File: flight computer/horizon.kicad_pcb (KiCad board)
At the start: 4 copper layers, 50.8 x 95.7 mm, 151 parts, among them J1 Micro_SD_Card_Det1, J10 Conn_01x02_Pin, J11 USB_C_Receptacle_USB2.0_16P, J12 Conn_01x04, J13 1x3 servo, J14 1x3 servo, J15 arming terminal, J16 arming terminal, J17 H9161TR-ND, J18 Conn_02x03_Counter_Clockwise, J19 Screw_Terminal_01x02, J20 Screw_Terminal_01x02, J21 Conn_02x03_Counter_Clockwise, J3 H9161TR-ND, J4 H9161TR-ND, J5 Screw_Term, J6 1x3 servo, J9 1x3 servo, Q2 DMG2301L, Q7 BSS138, Q8 IRLML6402, Q9 IRLML6402, SW1 CK_KMS2xxG, U1 MMCU, U10 LSM6DS3, U11 BGM220SC12WGA2R, U13 LTC4412xS6, U15 AP2112K-3.3, U16 SX1262IMLTRT, U17 PE4259, U2 MKL02Z32VFG4, U3 TPS61200DRC, U5 LPS22HB, U6 GPS, U8 NAND, U9 TPS82130, Y1 Crystal, Y2 32MHz

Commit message: i forgot what i did
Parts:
- moved Q7 17.3 mm to (187.5, 139.7)
- moved R72 17.3 mm to (191.2, 138.0)
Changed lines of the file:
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@@
 			(psa4output no)
 			(plot_black_and_white yes)
+			(plotinvisibletext no)
 			(sketchpadsonfab no)
 			(plotpadnumbers no)
@@
 	(footprint "Package_TO_SOT_SMD:SOT-23"
 		(layer "F.Cu")
-		(at 204.6175 141.79)
+		(at 187.4575 139.66)
 		(descr "SOT, 3 Pin (JEDEC TO-236 Var AB https://www.jedec.org/document_search?search_api_views_fulltext=TO-236), generated with kicad-footprint-generator ipc_gullwing_generator.py")
 		(tags "SOT TO_SOT_SMD")
@@
 	(footprint "Resistor_SMD:R_0603_1608Metric"
 		(layer "F.Cu")
-		(at 208.38 140.125 90)
+		(at 191.22 137.995 90)
 		(descr "Resistor SMD 0603 (1608 Metric), square (rectangular) end terminal, IPC_7351 nominal, (Body size source: IPC-SM-782 page 72, https://www.pcb-3d.com/wordpress/wp-content/uploads/ipc-sm-782a_amendment_1_and_2.pdf), generated with kicad-footprint-generator")
 		(tags "resistor")

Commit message: gotta get those daily commits in
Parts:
- moved R55 34.6 mm to (193.3, 88.6), turned to 0 degrees
- moved C15 33.7 mm to (191.0, 89.5), turned to 90 degrees
- moved R54 29.4 mm to (191.0, 92.6), turned to 90 degrees
- moved J1 29.2 mm to (196.5, 92.4), turned to 180 degrees
- moved U8 29.2 mm to (196.5, 92.4), turned to 180 degrees
- moved R12 28.8 mm to (202.0, 93.9), turned to 90 degrees
- moved R56 25.9 mm to (204.3, 97.2), turned to 90 degrees
- moved C47 10.7 mm to (180.7, 95.4)
- moved FL1 10.7 mm to (184.7, 95.6)
- moved R8 10.7 mm to (187.2, 89.0)
- moved C46 10.7 mm to (187.1, 92.1)
- moved C48 10.7 mm to (182.2, 95.4)
- moved L10 10.7 mm to (183.0, 97.7)
- moved U17 10.7 mm to (184.9, 92.7)
- moved C49 10.7 mm to (184.9, 89.6)
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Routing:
- net +3.3V: track 71.8 -> 141.7 mm
- net GND: track 119.2 -> 121.6 mm, vias 78 -> 80
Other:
- board size 50.8 x 95.7 mm -> 50.8 x 78 mm

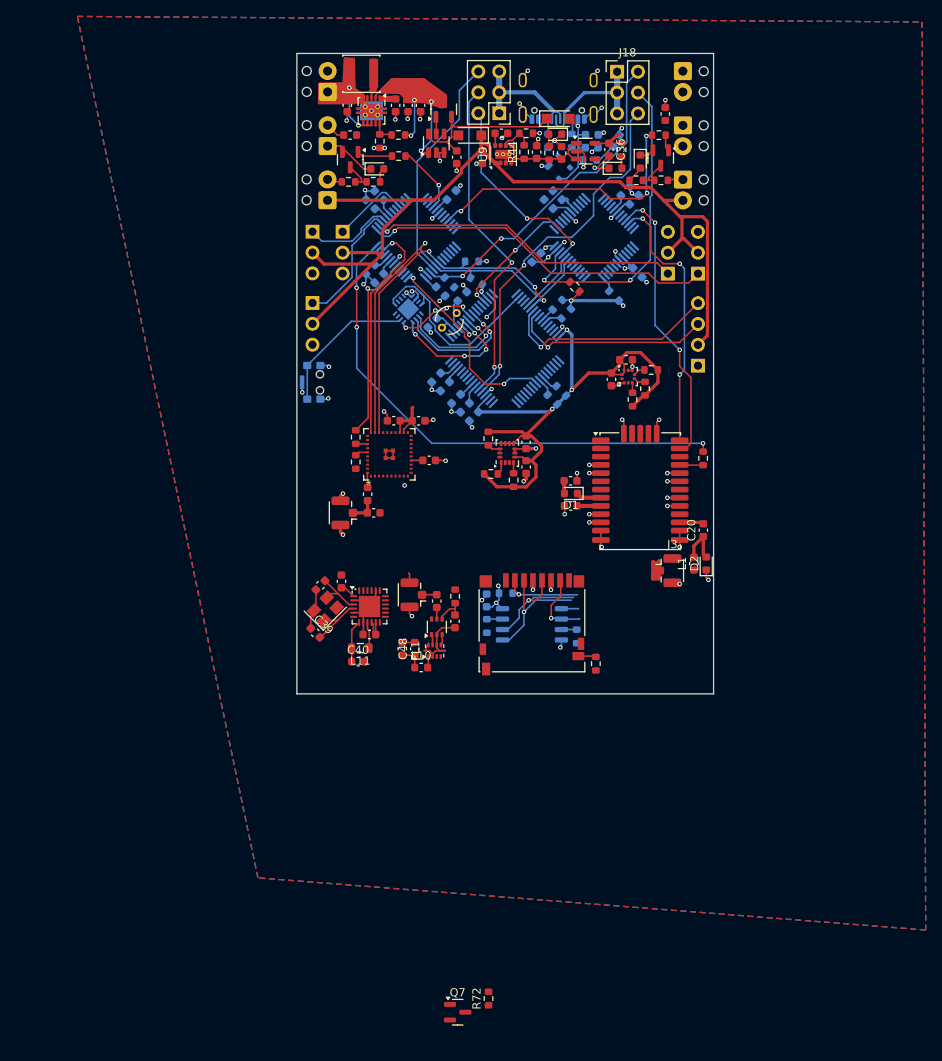
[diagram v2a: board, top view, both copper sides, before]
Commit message: work and updated from schematic
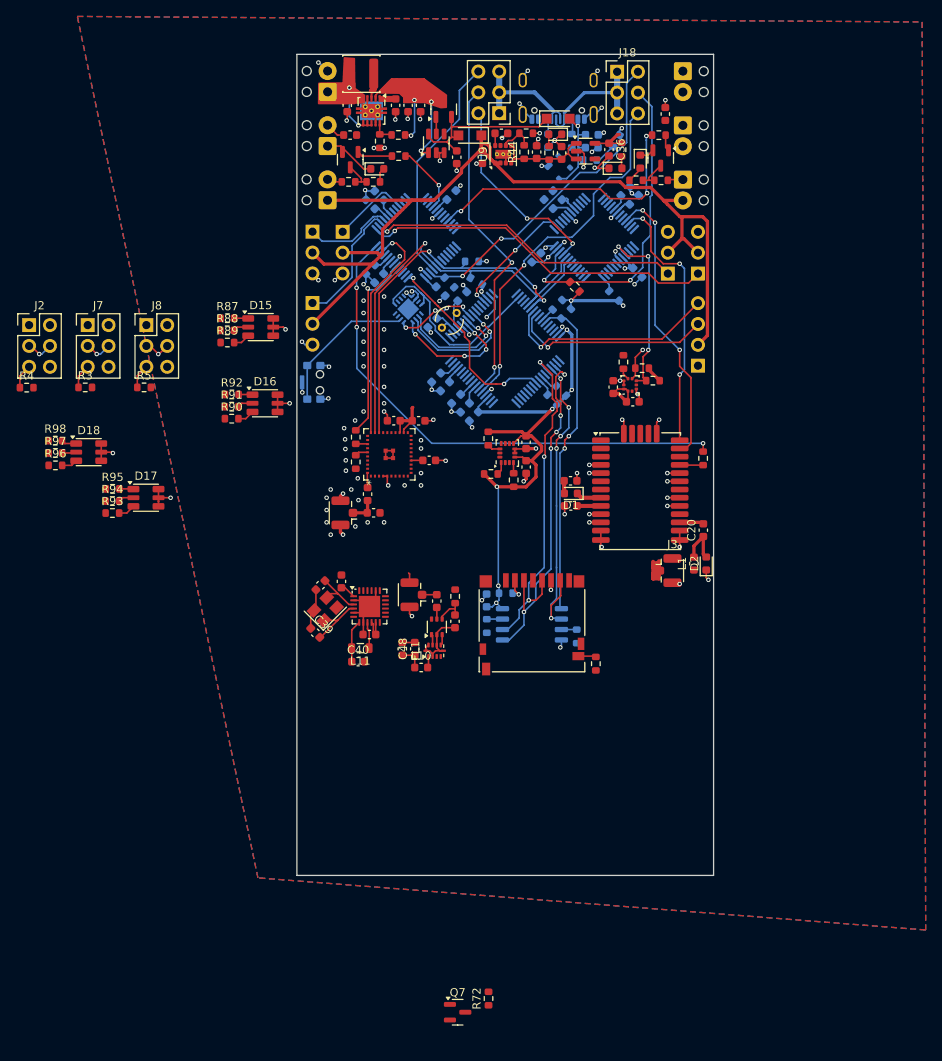
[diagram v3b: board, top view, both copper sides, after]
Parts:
- added D15: SMLVN6RGB, LED_SMD:LED_ROHM_SMLVN6, F.Cu at (163.5, 56.2)
- added D16: SMLVN6RGB, LED_SMD:LED_ROHM_SMLVN6, F.Cu at (164.0, 65.5)
- added D17: SMLVN6RGB, LED_SMD:LED_ROHM_SMLVN6, F.Cu at (149.5, 77.0)
- added D18: SMLVN6RGB, LED_SMD:LED_ROHM_SMLVN6, F.Cu at (142.5, 71.5)
- added J2: Conn_02x03_Counter_Clockwise, Connector_PinHeader_2.54mm:PinHeader_2x03_P2.54mm_Vertical, F.Cu at (135.3, 56.0)
- added J7: Conn_02x03_Counter_Clockwise, Connector_PinHeader_2.54mm:PinHeader_2x03_P2.54mm_Vertical, F.Cu at (142.4, 56.0)
- added J8: Conn_02x03_Counter_Clockwise, Connector_PinHeader_2.54mm:PinHeader_2x03_P2.54mm_Vertical, F.Cu at (149.5, 56.0)
- added R3: 10k, Resistor_SMD:R_0603_1608Metric, F.Cu at (142.1, 63.6)
- added R4: 10k, Resistor_SMD:R_0603_1608Metric, F.Cu at (135.0, 63.6)
- added R5: 10k, Resistor_SMD:R_0603_1608Metric, F.Cu at (149.3, 63.6)
- added R87: 220, Resistor_SMD:R_0603_1608Metric, F.Cu at (159.4, 55.1)
- added R88: 220, Resistor_SMD:R_0603_1608Metric, F.Cu at (159.4, 56.6)
- added R89: 220, Resistor_SMD:R_0603_1608Metric, F.Cu at (159.4, 58.1)
- added R90: 220, Resistor_SMD:R_0603_1608Metric, F.Cu at (159.9, 67.4)
- added R91: 220, Resistor_SMD:R_0603_1608Metric, F.Cu at (159.9, 65.9)
- added R92: 220, Resistor_SMD:R_0603_1608Metric, F.Cu at (160.0, 64.4)
- added R93: 220, Resistor_SMD:R_0603_1608Metric, F.Cu at (145.4, 78.9)
- added R94: 220, Resistor_SMD:R_0603_1608Metric, F.Cu at (145.4, 77.4)
- added R95: 220, Resistor_SMD:R_0603_1608Metric, F.Cu at (145.4, 75.9)
- added R96: 220, Resistor_SMD:R_0603_1608Metric, F.Cu at (138.5, 73.1)
- added R97: 220, Resistor_SMD:R_0603_1608Metric, F.Cu at (138.5, 71.5)
- added R98: 220, Resistor_SMD:R_0603_1608Metric, F.Cu at (138.5, 70.0)
- moved C51 3.77 mm to (208.8, 65.3), turned to 180 degrees
- moved C50 3.68 mm to (206.4, 63.5), turned to -90 degrees
- moved R52 3.52 mm to (207.6, 60.5), turned to -90 degrees
- moved R53 3.38 mm to (211.2, 62.7), turned to 180 degrees
- moved R39 2.52 mm to (209.9, 61.2), turned to 180 degrees
- moved U5 1.04 mm to (208.5, 63.3), turned to 90 degrees
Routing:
- net CS_NAND MMCU: track 4.32 -> 39.6 mm, vias 0 -> 2
- net GND: track 121.6 -> 154.1 mm, vias 80 -> 127
- net NAND_MISO MMCU: track 8.61 -> 38.6 mm, vias 1 -> 5
- net NAND_MOSI MMCU: track 15.2 -> 42.8 mm, vias 1 -> 5
- net SPI0_SCK MMCU: track 14.5 -> 41.7 mm, vias 1 -> 3
- net MISO TMCU: track 2.77 -> 23.7 mm, vias 0 -> 3
- net CS_SD MMCU: track 11.7 -> 4.54 mm
- net +3.3V: track 141.7 -> 137.4 mm
- net nRESET MMCU: track 25.5 -> 28.5 mm
- net nRESET DMCU-1: track 0.00 -> 2.98 mm
- net nRESET DMCU-2: track 0.00 -> 2.96 mm
- net CS_BARO TMCU: track 1.44 -> 4.04 mm, vias 0 -> 1
- net Net-(D17-GA): track 0.00 -> 2.08 mm
- net Net-(D16-GA): track 0.00 -> 2.05 mm
- net Net-(D15-GA): track 0.00 -> 2.05 mm
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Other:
- board size 50.8 x 78 mm -> 50.8 x 100 mm

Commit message: review please before power rails
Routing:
- net +3.3V: track 137.4 -> 184.6 mm
- net GND: track 154.1 -> 160.3 mm, vias 127 -> 130
- net D+: track 15.7 -> 21.9 mm
- net D-: track 15.2 -> 20.2 mm
- net +5V: track 121.5 -> 117.5 mm
- net MISO TMCU: track 23.7 -> 21.4 mm
- net I2C0_SCL: track 53.4 -> 51.3 mm
- net D- DMCU-2: track 24.0 -> 22.5 mm
- net PTD4: track 23.9 -> 22.6 mm
- net I2C0_SDA: track 52.8 -> 51.5 mm
- net NAND_MOSI MMCU: track 42.8 -> 41.6 mm
- net mosfet2_signalfire: track 34.4 -> 33.4 mm
- net D- MMCU: track 40.4 -> 41.0 mm
- net D+ DMCU-2: track 39.6 -> 39.0 mm

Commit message: did a lot of wiring stuffs
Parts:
- moved C14 19.3 mm to (171.3, 107.0)
- moved C37 19.3 mm to (177.2, 113.0)
- moved C38 19.3 mm to (173.8, 106.5)
- moved C39 19.3 mm to (170.6, 112.8)
- moved C40 19.3 mm to (175.9, 116.3)
- moved C46 19.3 mm to (187.7, 111.4)
- moved C47 19.3 mm to (181.2, 114.7)
- moved C48 19.3 mm to (182.8, 114.7)
- moved C49 19.3 mm to (185.4, 108.9)
- moved FL1 19.3 mm to (185.2, 115.0)
- moved J4 19.3 mm to (182.6, 108.1)
- moved L10 19.3 mm to (183.5, 117.0)
- moved L11 19.3 mm to (176.1, 114.6)
- moved R8 19.3 mm to (187.7, 108.3)
- moved U16 19.3 mm to (177.2, 109.6)
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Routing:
- net +3.3V: track 184.6 -> 168.8 mm
- net NAND_MISO MMCU: track 38.6 -> 33.7 mm, vias 5 -> 3
- net CS_NAND MMCU: track 39.6 -> 35.0 mm
- net SPI0_SCK MMCU: track 41.2 -> 36.6 mm
- net NAND_MOSI MMCU: track 41.6 -> 38.0 mm, vias 5 -> 3
- net +5V: track 117.5 -> 114.6 mm
- net GND: track 160.3 -> 157.4 mm, vias 130 -> 132

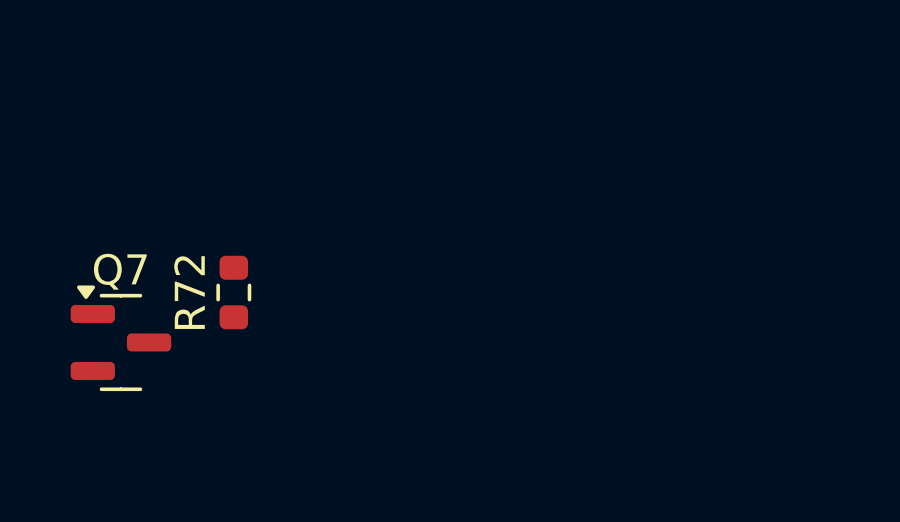
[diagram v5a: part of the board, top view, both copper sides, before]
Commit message: added buzzer footprint
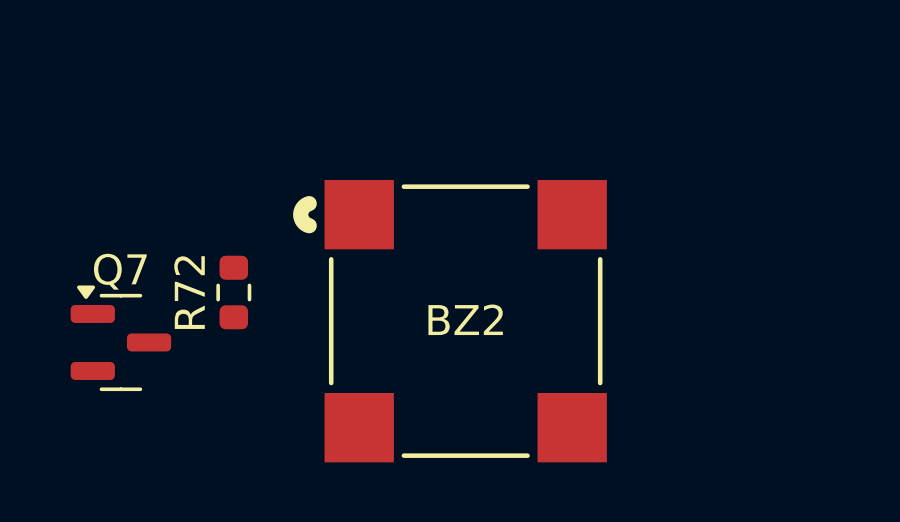
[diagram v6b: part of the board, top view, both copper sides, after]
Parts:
- added BZ2: Buzzer, Buzzer:MLT-8530_JHE, F.Cu at (198.9, 138.9)
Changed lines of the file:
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@@
 		)
+	)
+	(footprint "Buzzer:MLT-8530_JHE"
+		(layer "F.Cu")
+		(at 198.949999 138.949999)
+		(tags "MLT-8530 ")
+		(property "Reference" "BZ2"
+			(at 0 0 0)
+			(unlocked yes)
+			(layer "F.SilkS")
+			(effects
+				(font
+					(size 1 1)
+					(thickness 0.15)
+				)
+			)
+		)
+		(property "Value" "Buzzer"
+			(at 0 0 0)
+			(unlocked yes)
+			(layer "F.Fab")
+			(effects
+				(font
+					(size 1 1)
+					(thickness 0.15)
+				)
+			)
+		)
+		(property "Datasheet" "MLT-8530"
+			(at 0 0 0)
+			(layer "F.Fab")
+			(hide yes)
+			(effects
+				(font
+					(size 1.27 1.27)
+					(thickness 0.15)
+				)
+			)
+		)
+		(property "Description" "Buzzer, polarized"
+			(at 0 0 0)
+			(layer "F.Fab")
+			(hide yes)
+			(effects
+				(font
+					(size 1.27 1.27)
+					(thickness 0.15)
+				)
+			)
+		)
+		(property ki_fp_filters "MLT-8530_JHE")
+		(sheetname "/sensors/")
+		(sheetfile "sensor.kicad_sch")
+		(attr smd)
+		(fp_line
+			(start -4.4831 -2.061561)
+			(end -4.4831 2.061561)
+			(stroke
+				(width 0.1524)
+				(type solid)
+			)
+			(layer "F.SilkS")
+		)
+		(fp_line
+			(start -2.061561 4.4831)
+			(end 2.061561 4.4831)
+			(stroke
+				(width 0.1524)
+				(type solid)
+			)
+			(layer "F.SilkS")
+		)
+		(fp_line
+			(start 2.061561 -4.4831)
+			(end -2.061561 -4.4831)
+			(stroke
+				(width 0.1524)
+				(type solid)
+			)
+			(layer "F.SilkS")
+		)
+		(fp_line
+			(start 4.4831 2.061561)
+			(end 4.4831 -2.061561)
+			(stroke
+				(width 0.1524)
+				(type solid)
+			)
+			(layer "F.SilkS")
+		)
+		(fp_arc
+			(start -5.21624 -3.181857)
+			(mid -5.4991 -3.55)
+			(end -5.21624 -3.918144)
+			(stroke
+				(width 0.508)
+				(type solid)
+			)
+			(layer "F.SilkS")
+		)
+		(fp_circle
+			(center -5.1181 -3.55)
+			(end -4.7371 -3.55)
+			(stroke
+				(width 0.508)
+				(type solid)
+			)
+			(fill no)
+			(layer "B.SilkS")
+		)
+		(fp_line
+			(start -4.9597 -4.9597)
+			(end -4.9597 4.9597)
+			(stroke
+				(width 0.1524)
+				(type solid)
+			)
+			(layer "F.CrtYd")
+		)
+		(fp_line
+			(start -4.9597 4.9597)
+			(end 4.9597 4.9597)
+			(stroke
+				(width 0.1524)
+				(type solid)
+			)
+			(layer "F.CrtYd")
+		)
+		(fp_line
+			(start 4.9597 -4.9597)
+			(end -4.9597 -4.9597)
+			(stroke
+				(width 0.1524)
+				(type solid)
+			)
+			(layer "F.CrtYd")
+		)
+		(fp_line
+			(start 4.9597 4.9597)
+			(end 4.9597 -4.9597)
+			(stroke
+				(width 0.1524)
+				(type solid)
+			)
+			(layer "F.CrtYd")
+		)
+		(fp_line
+			(start -4.3561 -4.3561)
+			(end -4.3561 4.3561)
+			(stroke
+				(width 0.0254)
+				(type solid)
+			)
+			(layer "F.Fab")
+		)
+		(fp_line
+			(start -4.3561 4.3561)
+			(end 4.3561 4.3561)
+			(stroke
+				(width 0.0254)
+				(type solid)
+			)
+			(layer "F.Fab")
+		)
+		(fp_line
+			(start 4.3561 -4.3561)
+			(end -4.3561 -4.3561)
+			(stroke
+				(width 0.0254)
+				(type solid)
+			)
+			(layer "F.Fab")
+		)
+		(fp_line
+			(start 4.3561 4.3561)
+			(end 4.3561 -4.3561)
+			(stroke
+				(width 0.0254)
+				(type solid)
+			)
+			(layer "F.Fab")
+		)
+		(fp_circle
+			(center -3.55 -5.455)
+			(end -3.169 -5.455)
+			(stroke
+				(width 0.508)
+				(type solid)
+			)
+			(fill no)
+			(layer "F.Fab")
+		)
+		(fp_text user "${REFERENCE}"
+			(at 0 0 0)
+			(unlocked yes)
+			(layer "F.Fab")
+			(effects
+				(font
+					(size 1 1)
+					(thickness 0.15)
+				)
+			)
+		)
+		(pad "1" smd rect
+			(at -3.550001 -3.550001)
+			(size 2.3114 2.3114)
+			(layers "F.Cu" "F.Mask" "F.Paste")
+			(net 202 "Net-(Q7-D)")
+			(pinfunction "1")
+			(pintype "unspecified")
+		)
+		(pad "2" smd rect
+			(at -3.550001 3.550001)
+			(size 2.3114 2.3114)
+			(layers "F.Cu" "F.Mask" "F.Paste")
+			(net 2 "+3.3V")
+			(pinfunction "2")
+			(pintype "unspecified")
+		)
+		(pad "3" smd rect
+			(at 3.550001 -3.550001)
+			(size 2.3114 2.3114)
+			(layers "F.Cu" "F.Mask" "F.Paste")
+		)
+		(pad "4" smd rect
+			(at 3.550001 3.550001)
+			(size 2.3114 2.3114)
+			(layers "F.Cu" "F.Mask" "F.Paste")
+		)
+		(embedded_fonts no)
 	)
 	(footprint "Resistor_SMD:R_0603_1608Metric"
